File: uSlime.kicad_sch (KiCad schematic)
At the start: 0 parts

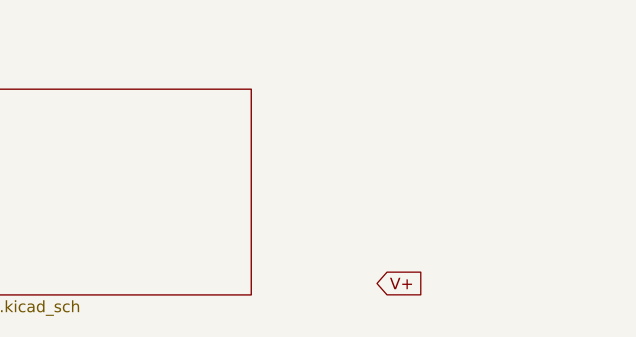
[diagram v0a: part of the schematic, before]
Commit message: Condense schematic
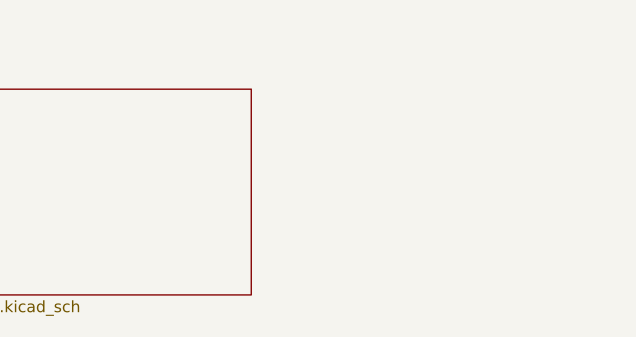
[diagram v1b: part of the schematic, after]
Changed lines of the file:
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@@
 	(generator_version "8.0")
 	(paper "A4")
-	(global_label "V+"
-		(shape input)
-		(at 157.48 102.87 0)
-		(fields_autoplaced yes)
-		(effects
-			(font
-				(size 1.27 1.27)
-			)
-			(justify left)
-		)
-		(property "Intersheetrefs" "${INTERSHEET_REFS}"
-			(at 163.1262 102.87 0)
-			(effects
-				(font
-					(size 1.27 1.27)
-				)
-				(justify left)
-				(hide yes)
-			)
-		)
-	)
 	(sheet
 		(at 104.14 81.28)
